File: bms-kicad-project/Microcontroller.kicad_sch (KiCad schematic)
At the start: 36 parts, among them J1 12402012E212A, J2 DEBUG, J3 Conn_02x18_Odd_Even, J4 Conn_02x18_Odd_Even, Q13 BSS308PE_H6327, SW1 KMR223G LFG, SW2 KMR223G LFG, U2 W25Q128JVSIQ TR, U3 NCP1117ST33T3G, U4 RP2040, X1 ABM8-272-T3

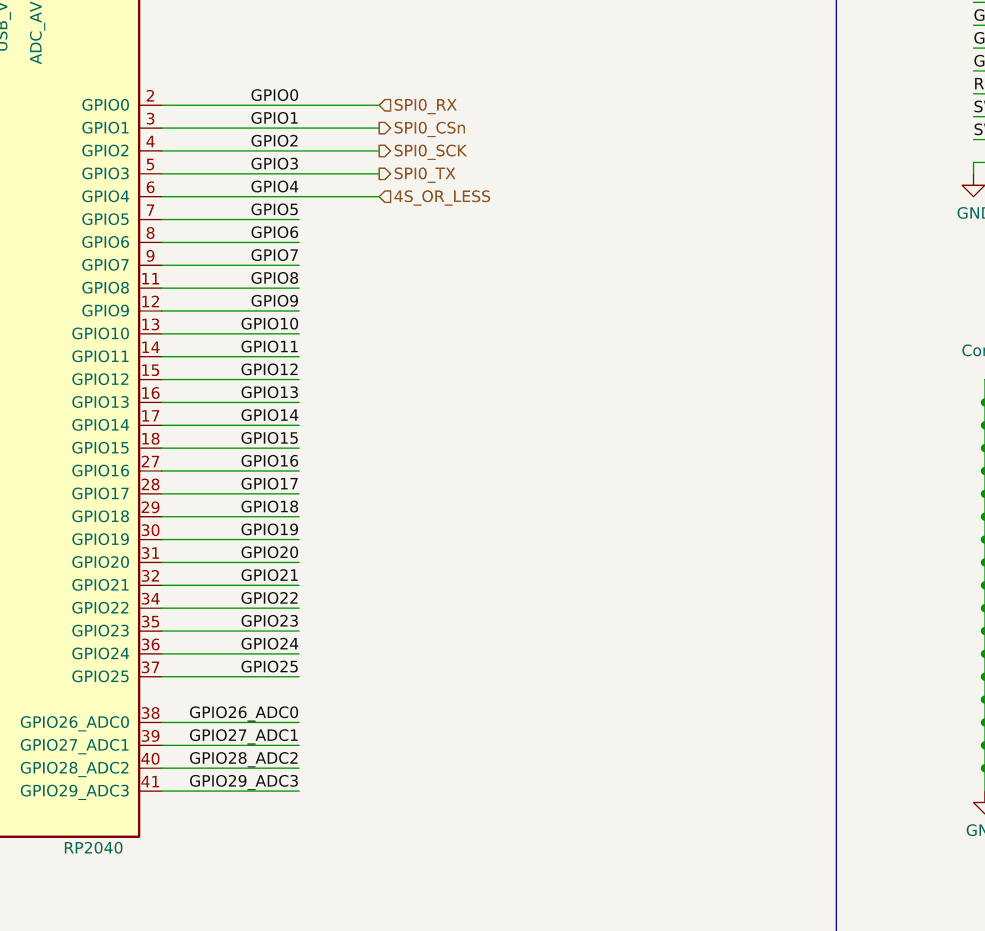
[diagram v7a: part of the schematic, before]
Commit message: feat: started a new sheet for external connections and added current sensor
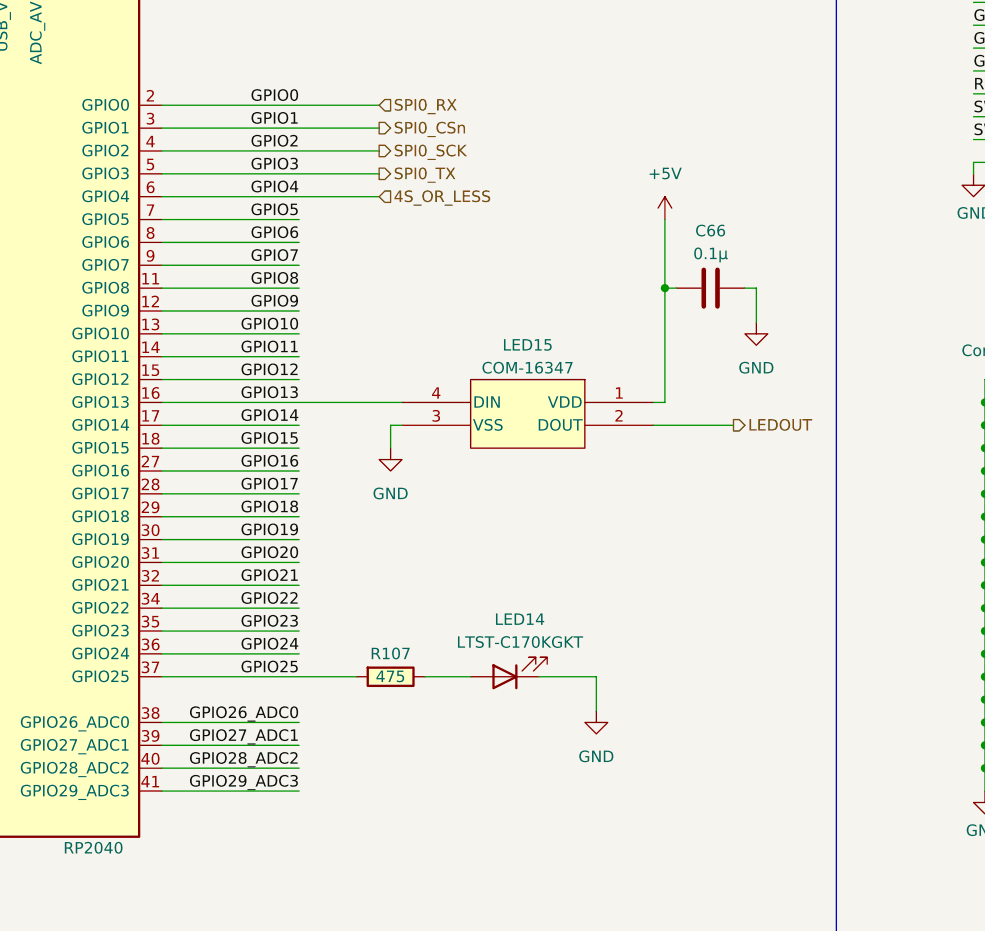
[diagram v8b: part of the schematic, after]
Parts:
- added C66: 0.1µ, FixedWing:G-21_MUR, symbol FixedWing:GCM21BR72A104KA37L
- added LED14: LTST-C170KGKT, FixedWing:LED_LTST-C170KGKT_LTO, symbol FixedWing:LTST-C170KGKT
- added LED15: COM-16347, FixedWing:COM-16347_SPK, symbol FixedWing:COM-16347
- added R107: 475, RESC2012X50N, symbol FixedWing:CRCW0805475RFKEA
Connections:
- net +5V: now also C66.2, LED15.1 (VDD)
- net GND: now also C66.1, LED14.1 (K), LED15.3 (VSS)
- net GPIO13: now also LED15.4 (DIN)
- net GPIO25: now also R107.1
- new net: LED14.2 (A), R107.2
- new net LEDOUT: LED15.2 (DOUT)
